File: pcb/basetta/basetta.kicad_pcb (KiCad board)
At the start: 2 copper layers, 56 x 35 mm, 36 parts, among them P1 batteria (2813), P10 cavo piatto, P11 uscita di X3, P2 2813, P3 abilitazione (D2 in linea), P4 seriale SSC-32, P5 bus GND, P6 bus 3V3, P7 bus SDA, P8 bus SCL, P9 dato delle luci delle tibie, U1 ESP32-S3-CAM RE1.3, U2 D24V22F5, U3 SN74AHCT125N

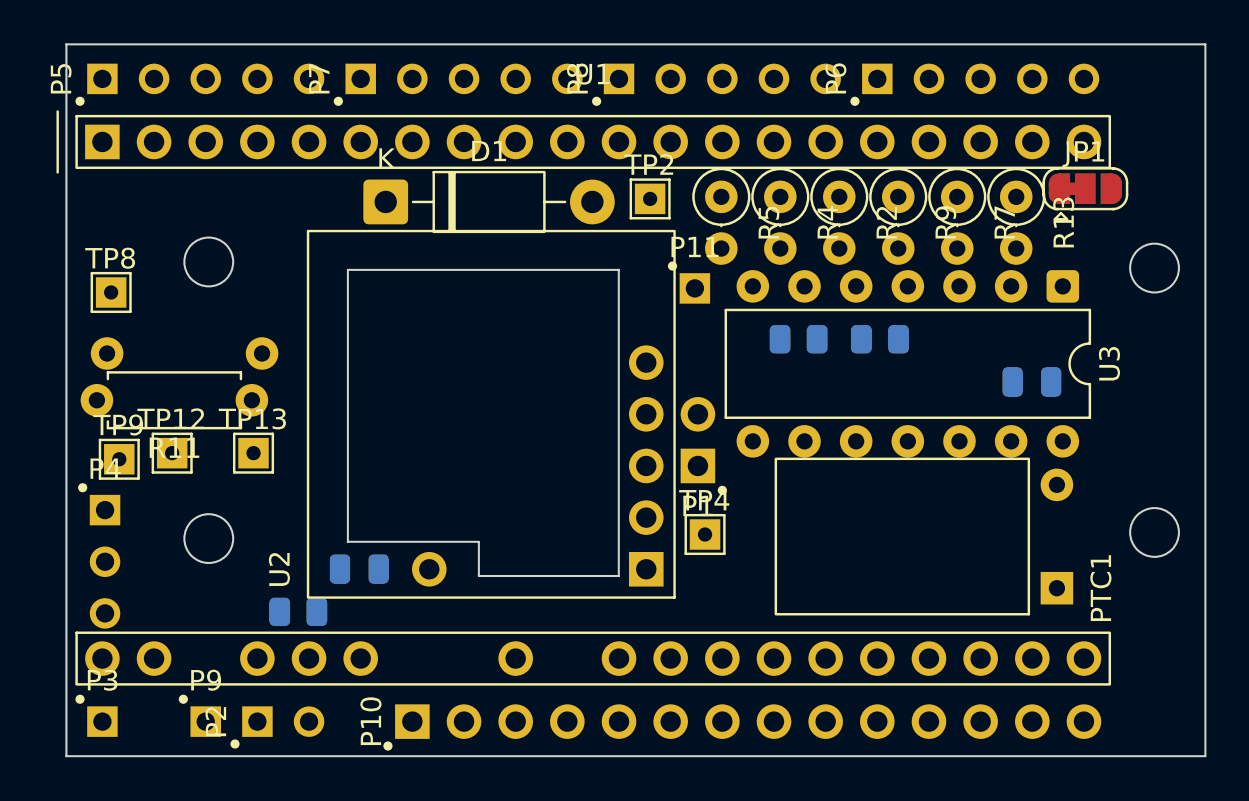
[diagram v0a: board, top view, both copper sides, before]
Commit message: D-083: dima della PCB-C; PCB-B piazzata e sbrogliata a quattro strati (scelta dell'utente) con DRC a zero: instradatore del progetto (script/sbroglio.py) per le reti con regole a coppie, Freerouting 2.5.0 per le altre, rifinitura; PTC MF-R090-0-9, 0805 sotto, resistenze in piedi, varchi 27/28/30/40, polo 14 tagliato, 3V3 a 0,3; ingombri nel CAD senza urti; dima e stampe
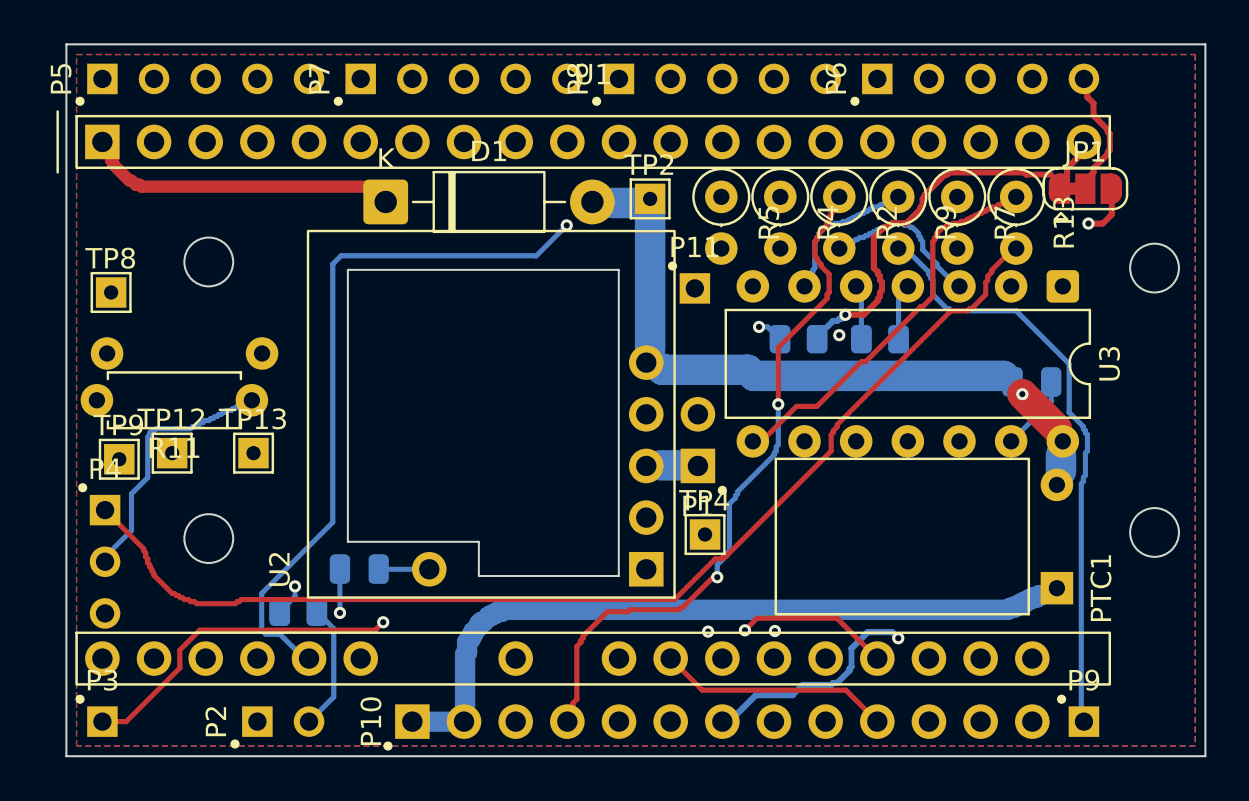
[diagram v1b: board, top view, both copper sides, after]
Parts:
- P10: footprint hex2:Fili_1x14_P2.54mm_D1.7 -> hex2:Fili_1x13_P2.54mm_D1.7
- moved P9 43.2 mm to (172.0, 115.8)
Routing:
- net /GND: track 0.00 -> 163.6 mm
- net /SDA: track 0.00 -> 76.5 mm, vias 0 -> 1
- net /LED_IN: track 0.00 -> 73.5 mm
- net /SENSE: track 0.00 -> 65.2 mm, vias 0 -> 2
- net /SCL: track 0.00 -> 59.5 mm
- net /TX5: track 0.00 -> 53.9 mm
- net /3V3S: track 0.00 -> 53.4 mm, vias 0 -> 2
- net /GPIO42: track 0.00 -> 42.0 mm, vias 0 -> 2
- net /TX3: track 0.00 -> 42.0 mm, vias 0 -> 2
- net /OFF: track 0.00 -> 38.8 mm, vias 0 -> 1
- net /5V_LED: track 0.00 -> 33.7 mm
- net /DATA: track 0.00 -> 32.6 mm, vias 0 -> 2
- net /5V_REG: track 0.00 -> 28.2 mm, vias 0 -> 1
- net /DATA_TIBIE: track 0.00 -> 28.0 mm
- net /3V3_X3: track 0.00 -> 23.6 mm, vias 0 -> 1
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- added copper zone on B.Cu, net /GND
- added copper zone on F.Cu, net /GND
- added copper zone on In1.Cu, net /GND
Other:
- copper layers 2 -> 4

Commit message: PCB-B: serigrafia (nomi delle piazzole dei fili, polarita', nome e faccia nel tratto dell'antenna), stato 'sbroglio' con DRC a zero anche sulla serigrafia; test di ripetibilita' senza i poligoni dei riempimenti (cambiano di 1e-6 fra Linux e Mac)
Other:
- board text added: "1"
- board text added: "13"
- board text added: "3V3"
- board text added: "EN"
- board text added: "GND"
- board text added: "HEX2 BASETTA r1 LATO COMPONENTI testa ->"
- board text added: "K"
- board text added: "OFF"
- board text added: "SCL"
- board text added: "SDA"
- board text added: "SNS"
- board text added: "TIB"
- board text added: "TX RX GND"
- board text added: "VBAT"
